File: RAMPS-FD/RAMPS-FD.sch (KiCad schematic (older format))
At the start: 10 parts, among them M101 LOGO_OSHW, P102 RESET, Q101 DMN2075, SW101 RESET

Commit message: Changed fuse holders to Keystone 3568; specificy HCT instead of ACT logic
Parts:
- D101: symbol LED -> LED-RESCUE-RAMPS-FD
- FID1, FID2, FID3, M101: Populate (none) -> No
- P102: footprint w_pin_strip:pin_strip_2 -> Pin_Headers:Pin_Header_Straight_1x02
- SW101: footprint rmc:SW_6x6_MULTI -> rmc:SW_6x6_SMD
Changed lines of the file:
@@
 F 2 "rmc:OSHW_logo_2" H 6000 7250 60  0001 C CNN
 F 3 "" H 6100 7200 60  0001 C CNN
+F 4 "No" H 6100 7200 60  0001 C CNN "Populate"
 	1    6100 7200
 	1    0    0    -1
@@
 F 0 "SW101" H 9500 5250 50  0000 C CNN
 F 1 "RESET" H 9500 5020 50  0000 C CNN
-F 2 "rmc:SW_6x6_MULTI" H 9500 5100 60  0001 C CNN
+F 2 "rmc:SW_6x6_SMD" H 9500 5100 60  0001 C CNN
 F 3 "" H 9500 5100 60  0001 C CNN
 	1    9500 5100
@@
 $EndComp
 $Comp
-L LED D101
+L LED-RESCUE-RAMPS-FD D101
 U 1 1 50FC24D8
 P 7950 4450
@@
 F 0 "P102" V 10300 5100 40  0000 C CNN
 F 1 "RESET" V 10400 5100 40  0000 C CNN
-F 2 "w_pin_strip:pin_strip_2" H 10350 5100 60  0001 C CNN
+F 2 "Pin_Headers:Pin_Header_Straight_1x02" H 10350 5100 60  0001 C CNN
 F 3 "" H 10350 5100 60  0000 C CNN
 	1    10350 5100
@@
 F 2 "Fiducials:Fiducial_1mm_Dia_2.54mm_Outer_CopperTop" H 10275 3675 60  0001 C CNN
 F 3 "" H 10375 3975 60  0000 C CNN
+F 4 "No" H 10375 3975 60  0001 C CNN "Populate"
 	1    10375 3975
 	1    0    0    -1
@@
 F 2 "Fiducials:Fiducial_1mm_Dia_2.54mm_Outer_CopperTop" H 10675 3675 60  0001 C CNN
 F 3 "" H 10775 3975 60  0000 C CNN
+F 4 "No" H 10775 3975 60  0001 C CNN "Populate"
 	1    10775 3975
 	1    0    0    -1
@@
 F 2 "Fiducials:Fiducial_1mm_Dia_2.54mm_Outer_CopperTop" H 9900 3675 60  0001 C CNN
 F 3 "" H 10000 3975 60  0000 C CNN
+F 4 "No" H 10000 3975 60  0001 C CNN "Populate"
 	1    10000 3975
 	1    0    0    -1

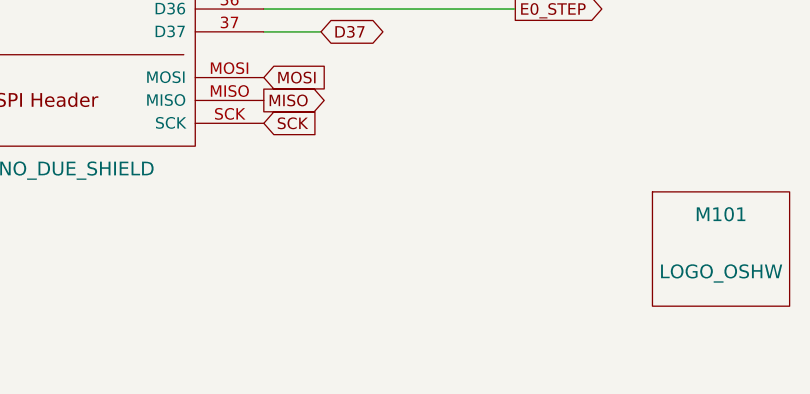
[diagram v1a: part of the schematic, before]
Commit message: Fix 3d view; remove faulty ADC protection
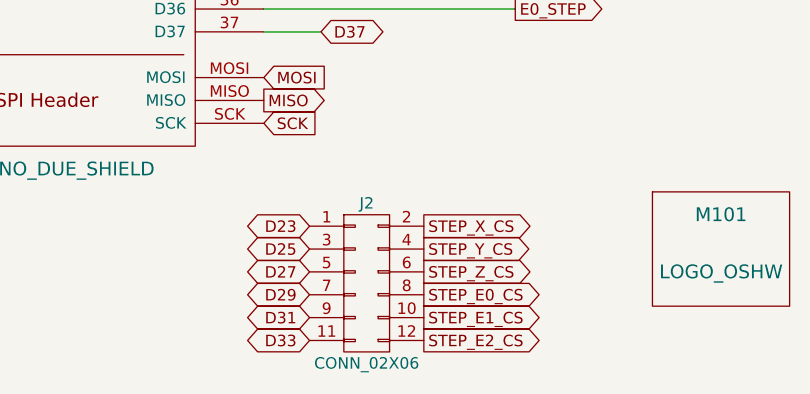
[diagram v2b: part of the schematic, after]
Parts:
- added J2: CONN_02X06, Pin_Headers:Pin_Header_Straight_2x06_Pitch2.54mm, symbol CONN_02X06
- P102: footprint Pin_Headers:Pin_Header_Straight_1x02 -> Pin_Headers:Pin_Header_Straight_1x02_Pitch2.54mm
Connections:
- net D23: now also J2.1 (P1)
- net D25: now also J2.3 (P3)
- net D27: now also J2.5 (P5)
- net D29: now also J2.7 (P7)
- net D31: now also J2.9 (P9)
- net D33: now also J2.11 (P11)
- new net STEP_E0_CS: J2.8 (P8)
- new net STEP_E1_CS: J2.10 (P10)
- new net STEP_E2_CS: J2.12 (P12)
- new net STEP_X_CS: J2.2 (P2)
- new net STEP_Y_CS: J2.4 (P4)
- new net STEP_Z_CS: J2.6 (P6)
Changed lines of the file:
@@
 F 0 "P102" V 10300 5100 40  0000 C CNN
 F 1 "RESET" V 10400 5100 40  0000 C CNN
-F 2 "Pin_Headers:Pin_Header_Straight_1x02" H 10350 5100 60  0001 C CNN
+F 2 "Pin_Headers:Pin_Header_Straight_1x02_Pitch2.54mm" H 10350 5100 60  0001 C CNN
 F 3 "" H 10350 5100 60  0000 C CNN
 	1    10350 5100
@@
 	1    0    0    -1
 $EndComp
+Text GLabel 4800 7200 2    50   Output ~ 0
+STEP_Y_CS
+$Comp
+L CONN_02X06 J2
+U 1 1 5B124015
+P 4550 7350
+F 0 "J2" H 4550 7700 50  0000 C CNN
+F 1 "CONN_02X06" H 4550 7000 50  0000 C CNN
+F 2 "Pin_Headers:Pin_Header_Straight_2x06_Pitch2.54mm" H 4550 6150 50  0001 C CNN
+F 3 "" H 4550 6150 50  0001 C CNN
+	1    4550 7350
+	1    0    0    -1
+$EndComp
+Text GLabel 4800 7100 2    50   Output ~ 0
+STEP_X_CS
+Text GLabel 4800 7300 2    50   Output ~ 0
+STEP_Z_CS
+Text GLabel 4800 7400 2    50   Output ~ 0
+STEP_E0_CS
+Text GLabel 4800 7500 2    50   Output ~ 0
+STEP_E1_CS
+Text GLabel 4800 7600 2    50   Output ~ 0
+STEP_E2_CS
+Text GLabel 4300 7600 0    50   BiDi ~ 0
+D33
+Text GLabel 4300 7500 0    50   BiDi ~ 0
+D31
+Text GLabel 4300 7400 0    50   BiDi ~ 0
+D29
+Text GLabel 4300 7300 0    50   BiDi ~ 0
+D27
+Text GLabel 4300 7200 0    50   BiDi ~ 0
+D25
+Text GLabel 4300 7100 0    50   BiDi ~ 0
+D23
 $EndSCHEMATC
